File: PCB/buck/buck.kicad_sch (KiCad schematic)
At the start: 1 part

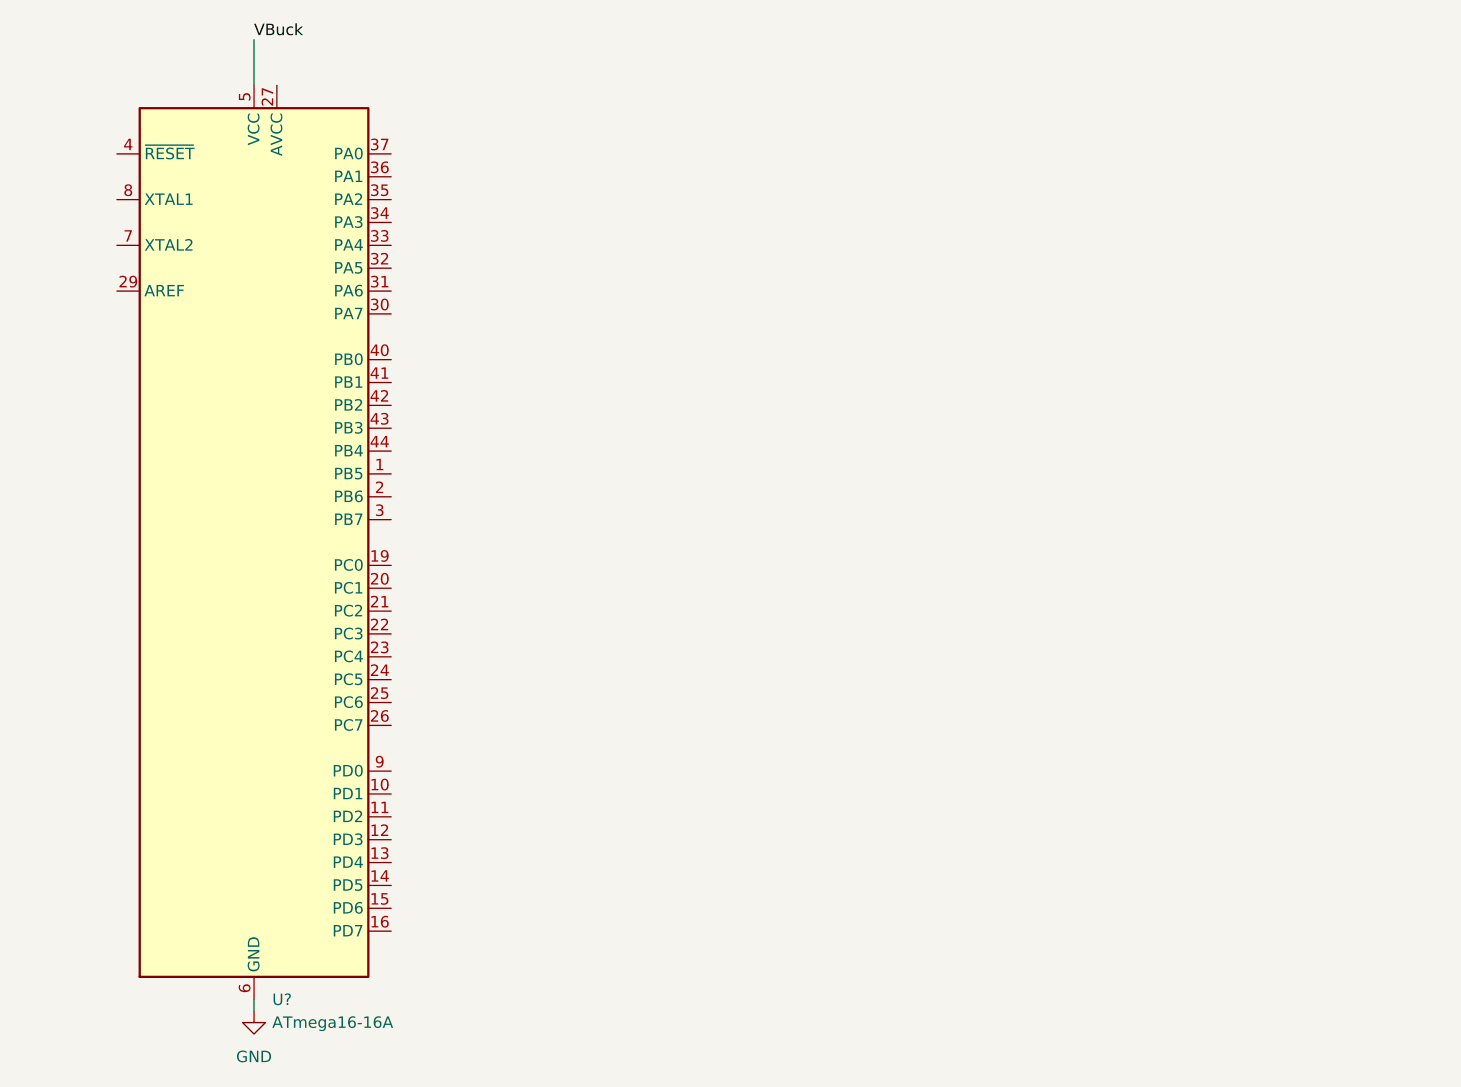
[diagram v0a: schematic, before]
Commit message: Fix missing PCB
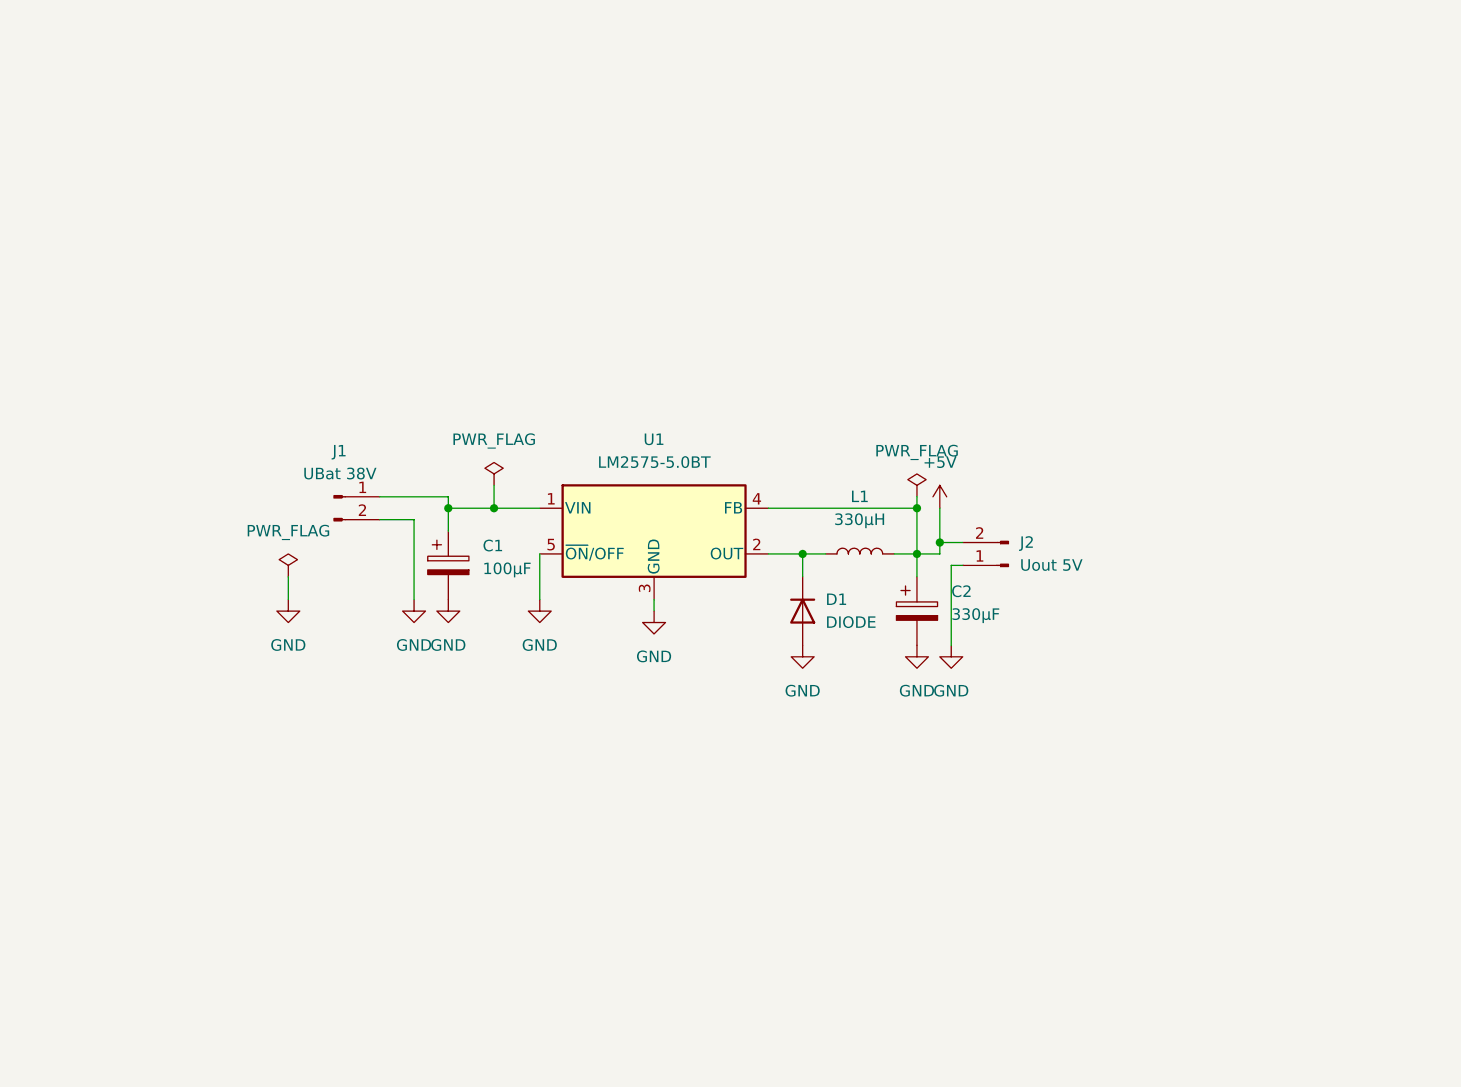
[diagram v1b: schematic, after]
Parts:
- removed U?: ATmega16-16A, Package_QFP:TQFP-44_10x10mm_P0.8mm, symbol MCU_Microchip_ATmega:ATmega16-16A
- added C1: 100µF, Capacitor_SMD:CP_Elec_8x10, symbol Device:C_Polarized
- added C2: 330µF, Capacitor_SMD:CP_Elec_10x10.5, symbol Device:C_Polarized
- added D1: DIODE, Diode_SMD:D_0805_2012Metric_Pad1.15x1.40mm_HandSolder, symbol Simulation_SPICE:DIODE
- added J1: UBat 38V, Connector_PinHeader_2.00mm:PinHeader_1x02_P2.00mm_Horizontal, symbol Connector:Conn_01x02_Male
- added J2: Uout 5V, Connector_PinHeader_2.00mm:PinHeader_1x02_P2.00mm_Vertical, symbol Connector:Conn_01x02_Male
- added L1: 330µH, Inductor_SMD:L_12x12mm_H8mm, symbol Device:L
- added U1: LM2575-5.0BT, Package_TO_SOT_THT:TO-220-5_Vertical, symbol Regulator_Switching:LM2575-5.0BT
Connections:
- net GND: now also C1.2, C2.2, D1.1 (A), J1.2 (Pin_2), J2.1 (Pin_1), U1.3 (GND), U1.5 (~{ON}/OFF)
- new net: C1.1, J1.1 (Pin_1), U1.1 (VIN)
- new net: D1.2 (K), L1.1, U1.2 (OUT)
- new net +5V: C2.1, J2.2 (Pin_2), L1.2, U1.4 (FB)

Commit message: Add files via upload
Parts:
- added H1, H2: MountingHole_Pad, MountingHole:MountingHole_2.7mm_M2.5_Pad, symbol Mechanical:MountingHole_Pad
- added J3: Zündung, Connector_PinSocket_2.54mm:PinSocket_1x01_P2.54mm_Horizontal, symbol Connector:Conn_01x01_Female
- added Q1: QM6006D, Package_TO_SOT_SMD:TO-252-2, symbol Transistor_FET:QM6006D
- added R1: 100k, Resistor_SMD:R_0805_2012Metric, symbol Device:R
- D1: value DIODE -> 1N4148
- J1: footprint Connector_PinHeader_2.00mm:PinHeader_1x02_P2.00mm_Horizontal -> Connector_PinSocket_2.54mm:PinSocket_1x02_P2.54mm_Horizontal
- J2: footprint Connector_PinHeader_2.00mm:PinHeader_1x02_P2.00mm_Vertical -> Connector_PinSocket_2.54mm:PinSocket_1x02_P2.54mm_Horizontal
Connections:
- net GND: now also H1.1, H2.1, Q1.2 (D); no longer J1.2 (Pin_2)
- new net: J1.2 (Pin_2), Q1.3 (S), R1.2
- new net: J3.1 (Pin_1), Q1.1 (G), R1.1
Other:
- moved on the sheet: J1

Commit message: Release v1.0
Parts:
- added R2, R3: 270k, Resistor_SMD:R_0805_2012Metric, symbol Device:R
- added R4, R5: 30k, Resistor_SMD:R_0805_2012Metric, symbol Device:R
- added R6, R7: 0R, Resistor_SMD:R_0603_1608Metric, symbol Device:R
- J2: footprint Connector_PinSocket_2.54mm:PinSocket_1x02_P2.54mm_Horizontal -> Connector_PinSocket_2.54mm:PinSocket_1x03_P2.54mm_Horizontal; symbol Connector:Conn_01x02_Male -> Connector:Conn_01x03_Female
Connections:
- net +5V: now also R7.1; no longer J2.2 (Pin_2)
- net GND: now also R5.2
- net at C1.1, J1.1 (Pin_1), U1.1 (VIN): now also R2.1
- new net: R3.2, R4.1, R6.1
- new net: R2.2, R3.1
- new net: J2.2 (Pin_2), R7.2
- new net: R4.2, R5.1
- new net ADC: J2.3 (Pin_3), R6.2
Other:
- moved on the sheet: C1, C2, D1, H1, H2, J1, J3, L1, Q1, R1, U1
